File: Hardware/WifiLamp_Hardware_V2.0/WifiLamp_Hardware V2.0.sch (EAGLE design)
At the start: 24 parts, among them CN1 MKDSN1,5/2-5,08, CN3 MKDSN1,5/2-5,08, CN4 MKDSN1,5/2-5,08, T1 BTA12, U1 LM1117, U2 MOC3041M

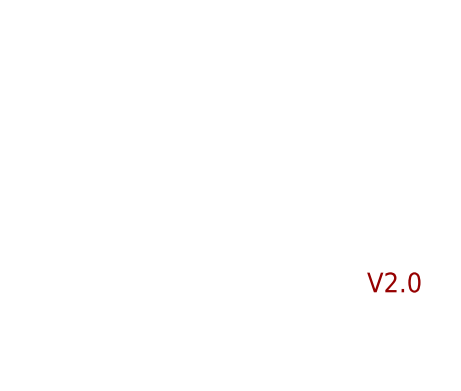
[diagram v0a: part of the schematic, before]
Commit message: Inclusão dos gerbers e BOM do hardware V2
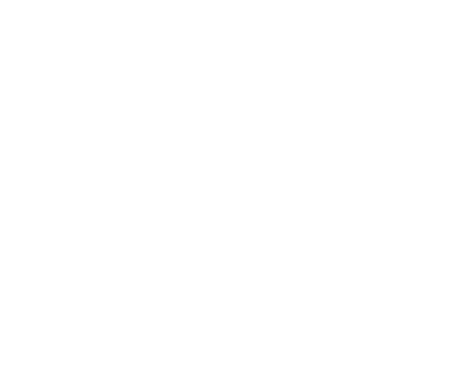
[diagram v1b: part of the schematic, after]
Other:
- note removed: "V2.0"
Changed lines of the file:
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@@
 <?xml version="1.0" encoding="utf-8"?>
 <!DOCTYPE eagle SYSTEM "eagle.dtd">
-<eagle version="7.6.0">
+<eagle version="7.7.0">
 <drawing>
 <settings>
@@
 <grid distance="0.1" unitdist="inch" unit="inch" style="lines" multiple="1" display="no" altdistance="0.01" altunitdist="inch" altunit="inch"/>
 <layers>
-<layer number="1" name="Top" color="4" fill="1" visible="yes" active="no"/>
-<layer number="16" name="Bottom" color="1" fill="1" visible="yes" active="no"/>
-<layer number="17" name="Pads" color="2" fill="1" visible="yes" active="no"/>
-<layer number="18" name="Vias" color="2" fill="1" visible="yes" active="no"/>
-<layer number="19" name="Unrouted" color="6" fill="1" visible="yes" active="no"/>
-<layer number="20" name="Dimension" color="15" fill="1" visible="yes" active="no"/>
-<layer number="21" name="tPlace" color="7" fill="1" visible="yes" active="no"/>
-<layer number="22" name="bPlace" color="7" fill="1" visible="yes" active="no"/>
-<layer number="23" name="tOrigins" color="15" fill="1" visible="yes" active="no"/>
-<layer number="24" name="bOrigins" color="15" fill="1" visible="yes" active="no"/>
-<layer number="25" name="tNames" color="7" fill="1" visible="yes" active="no"/>
-<layer number="26" name="bNames" color="7" fill="1" visible="yes" active="no"/>
-<layer number="27" name="tValues" color="7" fill="1" visible="yes" active="no"/>
-<layer number="28" name="bValues" color="7" fill="1" visible="yes" active="no"/>
+<layer number="1" name="Top" color="4" fill="1" visible="no" active="no"/>
+<layer number="16" name="Bottom" color="1" fill="1" visible="no" active="no"/>
+<layer number="17" name="Pads" color="2" fill="1" visible="no" active="no"/>
+<layer number="18" name="Vias" color="2" fill="1" visible="no" active="no"/>
+<layer number="19" name="Unrouted" color="6" fill="1" visible="no" active="no"/>
+<layer number="20" name="Dimension" color="15" fill="1" visible="no" active="no"/>
+<layer number="21" name="tPlace" color="7" fill="1" visible="no" active="no"/>
+<layer number="22" name="bPlace" color="7" fill="1" visible="no" active="no"/>
+<layer number="23" name="tOrigins" color="15" fill="1" visible="no" active="no"/>
+<layer number="24" name="bOrigins" color="15" fill="1" visible="no" active="no"/>
+<layer number="25" name="tNames" color="7" fill="1" visible="no" active="no"/>
+<layer number="26" name="bNames" color="7" fill="1" visible="no" active="no"/>
+<layer number="27" name="tValues" color="7" fill="1" visible="no" active="no"/>
+<layer number="28" name="bValues" color="7" fill="1" visible="no" active="no"/>
 <layer number="29" name="tStop" color="7" fill="3" visible="no" active="no"/>
 <layer number="30" name="bStop" color="7" fill="6" visible="no" active="no"/>
@@
 <layer number="35" name="tGlue" color="7" fill="4" visible="no" active="no"/>
 <layer number="36" name="bGlue" color="7" fill="5" visible="no" active="no"/>
-<layer number="37" name="tTest" color="7" fill="1" visible="yes" active="no"/>
-<layer number="38" name="bTest" color="7" fill="1" visible="yes" active="no"/>
+<layer number="37" name="tTest" color="7" fill="1" visible="no" active="no"/>
+<layer number="38" name="bTest" color="7" fill="1" visible="no" active="no"/>
 <layer number="39" name="tKeepout" color="4" fill="11" visible="no" active="no"/>
 <layer number="40" name="bKeepout" color="1" fill="11" visible="no" active="no"/>
@@
 <layer number="44" name="Drills" color="7" fill="1" visible="no" active="no"/>
 <layer number="45" name="Holes" color="7" fill="1" visible="no" active="no"/>
-<layer number="46" name="Milling" color="3" fill="1" visible="yes" active="no"/>
-<layer number="47" name="Measures" color="7" fill="1" visible="yes" active="no"/>
-<layer number="48" name="Document" color="7" fill="1" visible="yes" active="no"/>
-<layer number="49" name="Reference" color="7" fill="1" visible="yes" active="no"/>
-<layer number="51" name="tDocu" color="7" fill="1" visible="yes" active="no"/>
-<layer number="52" name="bDocu" color="7" fill="1" visible="yes" active="no"/>
+<layer number="46" name="Milling" color="3" fill="1" visible="no" active="no"/>
+<layer number="47" name="Measures" color="7" fill="1" visible="no" active="no"/>
+<layer number="48" name="Document" color="7" fill="1" visible="no" active="no"/>
+<layer number="49" name="Reference" color="7" fill="1" visible="no" active="no"/>
+<layer number="51" name="tDocu" color="7" fill="1" visible="no" active="no"/>
+<layer number="52" name="bDocu" color="7" fill="1" visible="no" active="no"/>
 <layer number="90" name="Modules" color="5" fill="1" visible="yes" active="yes"/>
 <layer number="91" name="Nets" color="2" fill="1" visible="yes" active="yes"/>
@@
 Embarcados
 Mazza-G Tec</text>
-<text x="250.19" y="15.24" size="2.1844" layer="94">V2.0</text>
 </plain>
 <instances>

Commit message: Inclusao do firmware e app
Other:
- note added: "V2.0"
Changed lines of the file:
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@@
 <?xml version="1.0" encoding="utf-8"?>
 <!DOCTYPE eagle SYSTEM "eagle.dtd">
-<eagle version="7.7.0">
+<eagle version="7.6.0">
 <drawing>
 <settings>
@@
 <grid distance="0.1" unitdist="inch" unit="inch" style="lines" multiple="1" display="no" altdistance="0.01" altunitdist="inch" altunit="inch"/>
 <layers>
-<layer number="1" name="Top" color="4" fill="1" visible="no" active="no"/>
-<layer number="16" name="Bottom" color="1" fill="1" visible="no" active="no"/>
-<layer number="17" name="Pads" color="2" fill="1" visible="no" active="no"/>
-<layer number="18" name="Vias" color="2" fill="1" visible="no" active="no"/>
-<layer number="19" name="Unrouted" color="6" fill="1" visible="no" active="no"/>
-<layer number="20" name="Dimension" color="15" fill="1" visible="no" active="no"/>
-<layer number="21" name="tPlace" color="7" fill="1" visible="no" active="no"/>
-<layer number="22" name="bPlace" color="7" fill="1" visible="no" active="no"/>
-<layer number="23" name="tOrigins" color="15" fill="1" visible="no" active="no"/>
-<layer number="24" name="bOrigins" color="15" fill="1" visible="no" active="no"/>
-<layer number="25" name="tNames" color="7" fill="1" visible="no" active="no"/>
-<layer number="26" name="bNames" color="7" fill="1" visible="no" active="no"/>
-<layer number="27" name="tValues" color="7" fill="1" visible="no" active="no"/>
-<layer number="28" name="bValues" color="7" fill="1" visible="no" active="no"/>
+<layer number="1" name="Top" color="4" fill="1" visible="yes" active="no"/>
+<layer number="16" name="Bottom" color="1" fill="1" visible="yes" active="no"/>
+<layer number="17" name="Pads" color="2" fill="1" visible="yes" active="no"/>
+<layer number="18" name="Vias" color="2" fill="1" visible="yes" active="no"/>
+<layer number="19" name="Unrouted" color="6" fill="1" visible="yes" active="no"/>
+<layer number="20" name="Dimension" color="15" fill="1" visible="yes" active="no"/>
+<layer number="21" name="tPlace" color="7" fill="1" visible="yes" active="no"/>
+<layer number="22" name="bPlace" color="7" fill="1" visible="yes" active="no"/>
+<layer number="23" name="tOrigins" color="15" fill="1" visible="yes" active="no"/>
+<layer number="24" name="bOrigins" color="15" fill="1" visible="yes" active="no"/>
+<layer number="25" name="tNames" color="7" fill="1" visible="yes" active="no"/>
+<layer number="26" name="bNames" color="7" fill="1" visible="yes" active="no"/>
+<layer number="27" name="tValues" color="7" fill="1" visible="yes" active="no"/>
+<layer number="28" name="bValues" color="7" fill="1" visible="yes" active="no"/>
 <layer number="29" name="tStop" color="7" fill="3" visible="no" active="no"/>
 <layer number="30" name="bStop" color="7" fill="6" visible="no" active="no"/>
@@
 <layer number="35" name="tGlue" color="7" fill="4" visible="no" active="no"/>
 <layer number="36" name="bGlue" color="7" fill="5" visible="no" active="no"/>
-<layer number="37" name="tTest" color="7" fill="1" visible="no" active="no"/>
-<layer number="38" name="bTest" color="7" fill="1" visible="no" active="no"/>
+<layer number="37" name="tTest" color="7" fill="1" visible="yes" active="no"/>
+<layer number="38" name="bTest" color="7" fill="1" visible="yes" active="no"/>
 <layer number="39" name="tKeepout" color="4" fill="11" visible="no" active="no"/>
 <layer number="40" name="bKeepout" color="1" fill="11" visible="no" active="no"/>
@@
 <layer number="44" name="Drills" color="7" fill="1" visible="no" active="no"/>
 <layer number="45" name="Holes" color="7" fill="1" visible="no" active="no"/>
-<layer number="46" name="Milling" color="3" fill="1" visible="no" active="no"/>
-<layer number="47" name="Measures" color="7" fill="1" visible="no" active="no"/>
-<layer number="48" name="Document" color="7" fill="1" visible="no" active="no"/>
-<layer number="49" name="Reference" color="7" fill="1" visible="no" active="no"/>
-<layer number="51" name="tDocu" color="7" fill="1" visible="no" active="no"/>
-<layer number="52" name="bDocu" color="7" fill="1" visible="no" active="no"/>
+<layer number="46" name="Milling" color="3" fill="1" visible="yes" active="no"/>
+<layer number="47" name="Measures" color="7" fill="1" visible="yes" active="no"/>
+<layer number="48" name="Document" color="7" fill="1" visible="yes" active="no"/>
+<layer number="49" name="Reference" color="7" fill="1" visible="yes" active="no"/>
+<layer number="51" name="tDocu" color="7" fill="1" visible="yes" active="no"/>
+<layer number="52" name="bDocu" color="7" fill="1" visible="yes" active="no"/>
 <layer number="90" name="Modules" color="5" fill="1" visible="yes" active="yes"/>
 <layer number="91" name="Nets" color="2" fill="1" visible="yes" active="yes"/>
@@
 Embarcados
 Mazza-G Tec</text>
+<text x="250.19" y="15.24" size="2.1844" layer="94">V2.0</text>
 </plain>
 <instances>
